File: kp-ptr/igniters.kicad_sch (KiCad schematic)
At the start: 52 parts, among them J10 Conn_01x02, J11 Conn_01x02, J12 Conn_01x02, J13 Conn_01x02, Q10 PMOS_SOT23, Q11 PMOS_SOT23, Q12 PMOS_SOT23, Q13 PMOS_SOT23, Q2 PMOS_SOT23, Q3 PMOS_SOT23, Q4 PMOS_SOT23, Q5 PMOS_SOT23, Q6 NMOS_SOT23, Q7 NMOS_SOT23, Q8 NMOS_SOT23, Q9 NMOS_SOT23

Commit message: Parts renumbered! Noice!
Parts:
- renumbered C48 to C55, C49 to C56, C47 to C57, C50 to C58, F3 to F2, F4 to F3, F2 to F4, J11 to J10, J12 to J11, J10 to J12, Q12 to Q10, Q4 to Q11, Q6 to Q12, Q7 to Q13, Q11 to Q2, Q2 to Q3, Q13 to Q4, Q9 to Q6, Q8 to Q7, Q10 to Q8, Q3 to Q9, R51 to R53, R60 to R54, R53 to R55, R62 to R56, R56 to R58, R70 to R59, R67 to R60, R49 to R61, R58 to R62, R45 to R63, R71 to R64, R54 to R65, R50 to R67, R61 to R68, R52 to R69, R63 to R70, R46 to R71, R47 to R72, R68 to R73, R72 to R74, R48 to R75, R59 to R76, R44 to R77, R69 to R78, R55 to R79, R73 to R80
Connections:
- net IGN1_DET: now also R61.1, R63.1; no longer R75.1, R77.1
- net IGN1_EN: now also Q6.1 (G), R57.1; no longer Q12.1 (G), R71.1
- net IGN3_DET: now also R75.1, R77.1; no longer R61.1, R63.1
- net IGN3_EN: now also Q12.1 (G), R71.1; no longer Q13.1 (G), R72.1
- net IGN4_EN: now also Q13.1 (G), R72.1; no longer Q6.1 (G), R57.1
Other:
- moved on the sheet: C55, C56, C57, C58, F2, F3, F4, F5, J10, J11, J12, J13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

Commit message: Release v1
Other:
- company: (none) -> Polskie Towarzystwo Rakietowe
- title: (none) -> KP-PTR
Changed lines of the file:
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@@
 (kicad_sch (version 20211123) (generator eeschema)
   (paper "A4")
+  (title_block
+    (title "KP-PTR")
+    (date "2022-11-18")
+    (rev "1")
+    (company "Polskie Towarzystwo Rakietowe")
+    (comment 1 "bartekM, FlyingBanana, Kretu, Red Labs, Stachu M, U.S. air force i inni")
+  )
   (junction (at 217.805 69.85) (diameter 0) (color 0 0 0 0)
   )

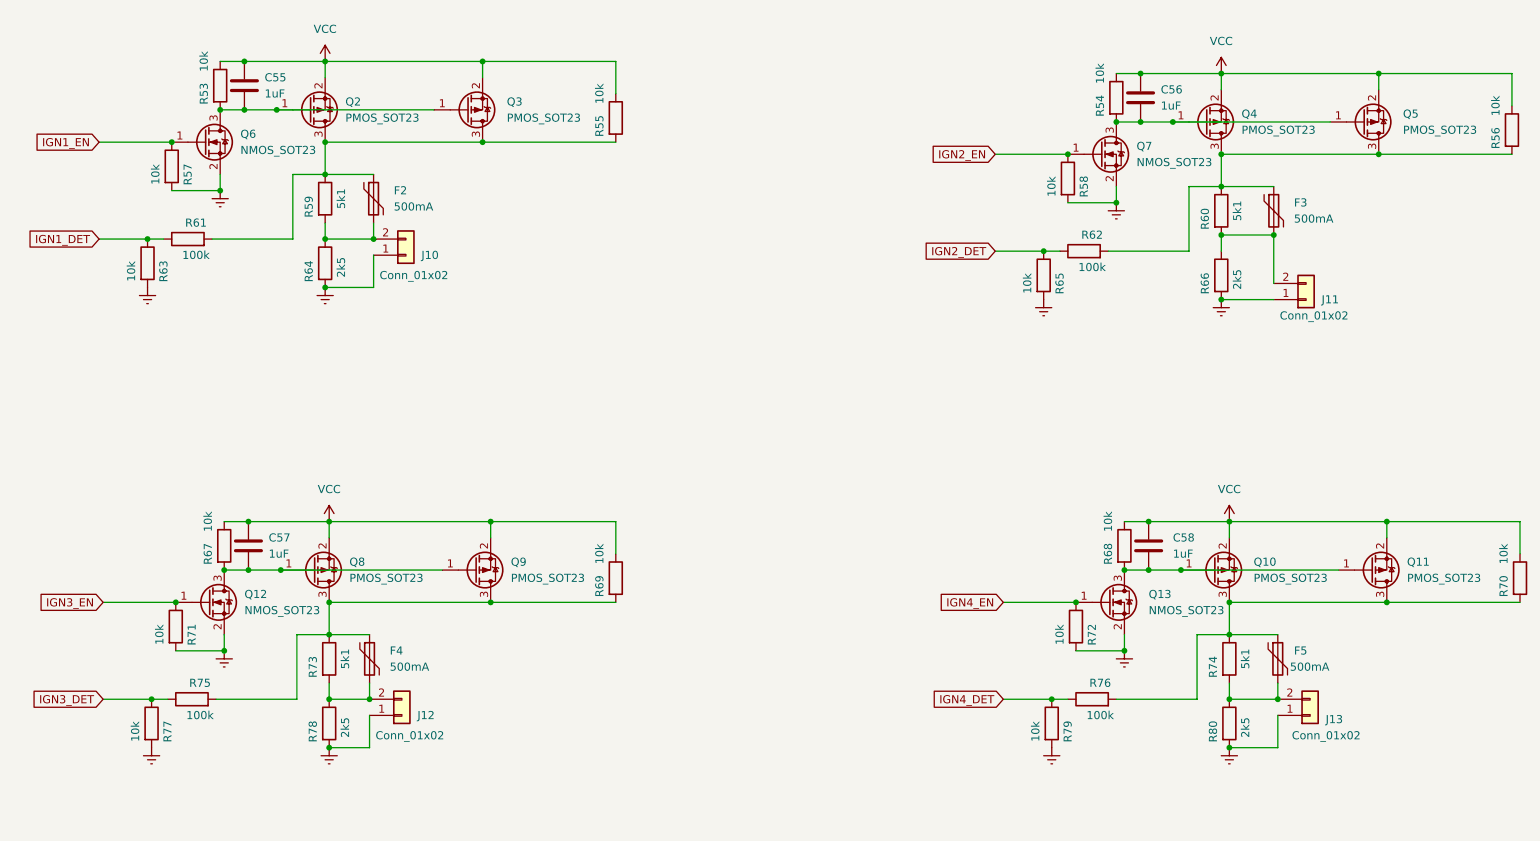
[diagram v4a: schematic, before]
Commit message: - Removed old teardrops polygons
- Removed unused LDO
- Removed unused LNA
+ DC-DC with additional capacitors
+ IGN connectors moved closer together
- removed additional unused resistors for igniter detection
+ small rearrangement of DC-DC etc
+ XTAL series 0R resistor changed to inductor
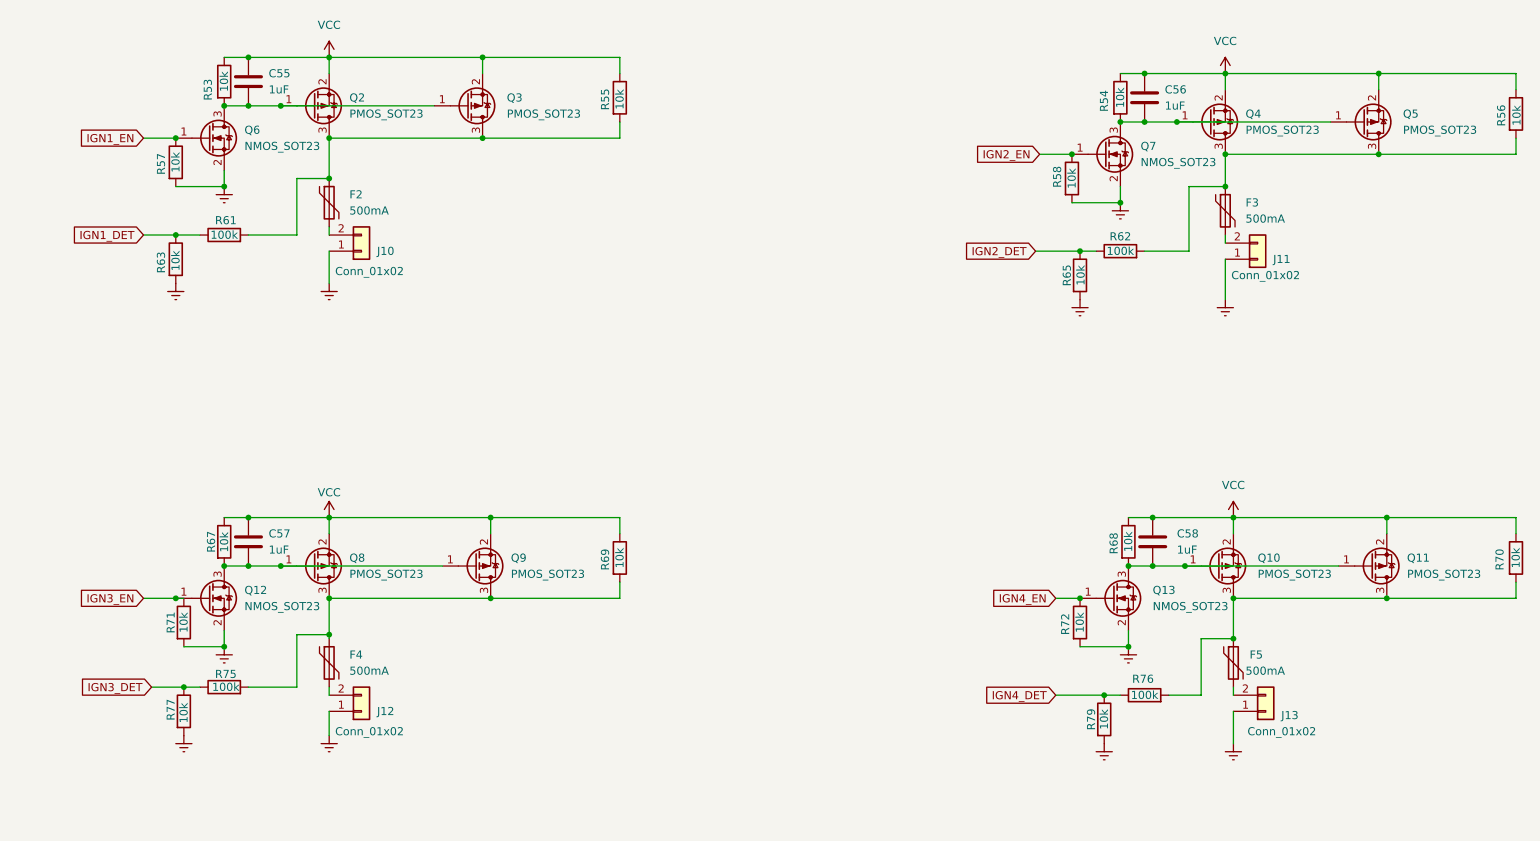
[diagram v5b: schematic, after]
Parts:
- removed R59, R60, R73, R74: 5k1, Resistor_SMD:R_0402_1005Metric, symbol Device:R
- removed R64, R66, R78, R80: 2k5, Resistor_SMD:R_0402_1005Metric, symbol Device:R
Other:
- moved on the sheet: C55, C56, C57, C58, F2, F3, F4, F5, J10, J11, J12, J13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
